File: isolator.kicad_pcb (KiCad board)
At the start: 4 copper layers, 120 x 50 mm, 54 parts, among them J1 HOST, J2 ISO_PORT, Q1 2N7002, T1 750313638, U1 ADuM4165, U2 USBLC6-2SC6, U3 USBLC6-2SC6, U4 SN6505BDBV, U5 TLV76750DGNR, U6 TPS2553DBV, Y1 24M 8pF

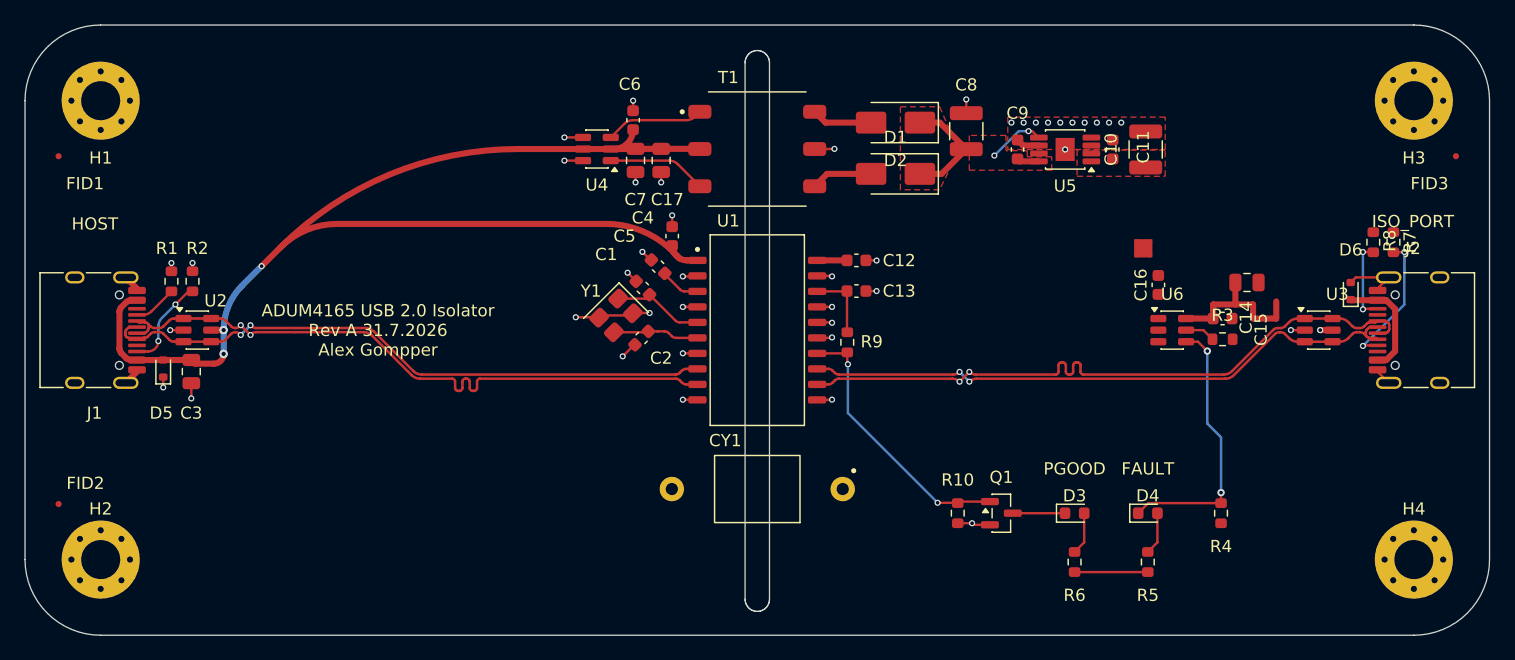
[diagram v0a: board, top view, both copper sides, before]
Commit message: wip: manual board re-import and placement pass
Hand work in the KiCad GUI after the C6 0805 change: schematic re-import,
board placement and routing. Committed as-is at Alex's request; not yet
re-verified against the gates.
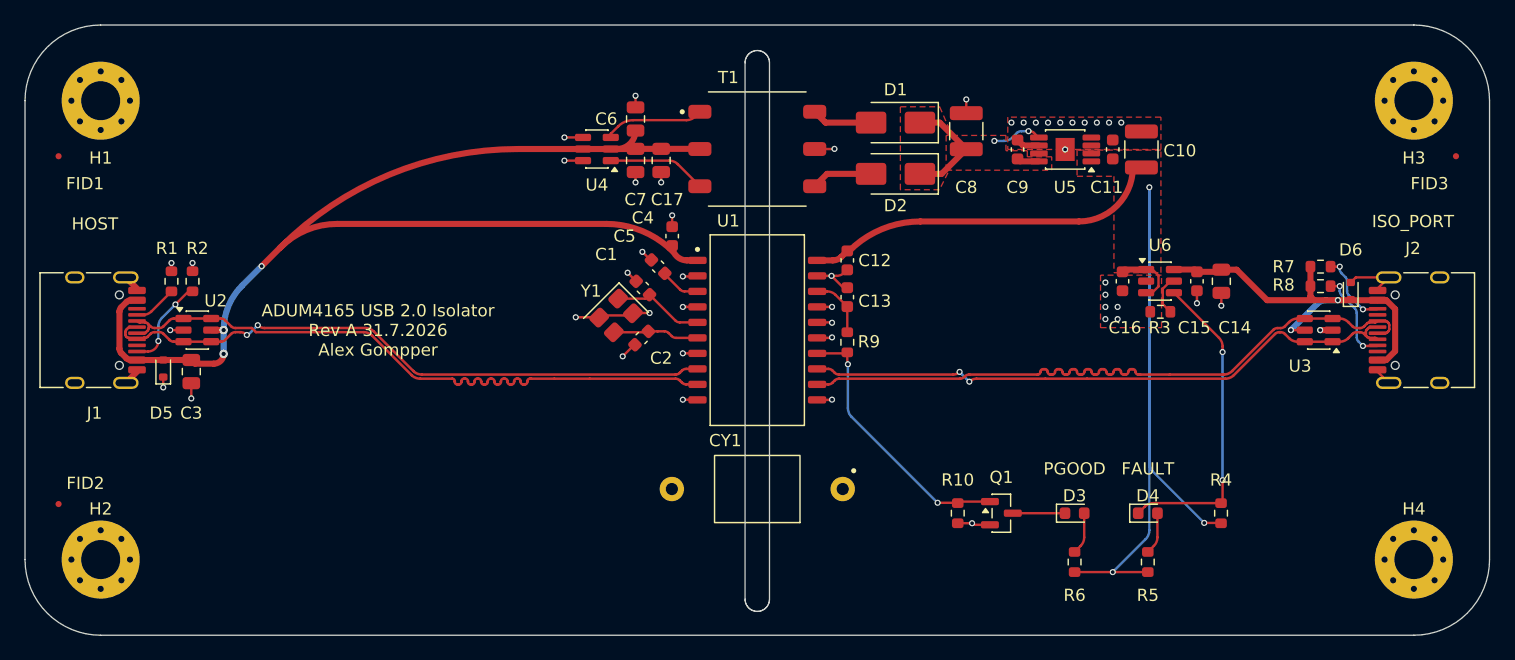
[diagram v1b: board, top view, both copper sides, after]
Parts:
- removed NT1: NetTie_4, NetTie:NetTie-4_SMD_Pad0.5mm
- removed NT3: NetTie_2, NetTie:NetTie-2_SMD_Pad0.5mm
- C6: footprint Capacitor_SMD:C_0603_1608Metric -> Capacitor_SMD:C_0805_2012Metric
- moved R7 6.30 mm to (193.0, 96.5), turned to 180 degrees
- moved R8 5.63 mm to (193.0, 98.1), turned to 0 degrees
- moved R3 5.57 mm to (179.9, 100.2)
- moved U6 4.14 mm to (179.9, 97.7)
- moved C15 3.71 mm to (182.9, 97.7), turned to -90 degrees
- moved C16 2.95 mm to (176.8, 97.7), turned to -90 degrees
- moved C14 2.10 mm to (184.9, 97.7), turned to -90 degrees
- moved C13 0.90 mm to (154.2, 99.0), turned to 90 degrees
- moved C12 0.75 mm to (154.2, 96.0), turned to -90 degrees
- moved C10 0.35 mm to (178.3, 86.9)
- moved C6 0.22 mm to (136.9, 84.4)
- turned R4 to -90 degrees
- turned U3 to 180 degrees
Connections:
- net /FAULT_LED_A renamed Net-(D4-A)
- C10 pad 1: /ISO_5V -> ISO_5V
- C11 pad 1: /ISO_5V -> ISO_5V
- C12 pad 1: /ISO_5V_VBUS2 -> ISO_5V
- C14 pad 1: /PORT_VBUS -> PORT_VBUS
- C15 pad 1: /PORT_VBUS -> PORT_VBUS
- C16 pad 1: /ISO_5V_SW -> ISO_5V
- D4 pad 1: /nFAULT -> Net-(D4-K)
- D6 pad 1: /PORT_VBUS_J2 -> PORT_VBUS
- J2 pad A4: /PORT_VBUS_J2 -> PORT_VBUS
- J2 pad A5: /PORT_CC1 -> Net-(J2-CC1)
- J2 pad A6: Net-(J2-D+-PadA6) -> /PORT_D+
- J2 pad A7: Net-(J2-D--PadA7) -> /PORT_D-
- J2 pad A9: /PORT_VBUS_J2 -> PORT_VBUS
- J2 pad B4: /PORT_VBUS_J2 -> PORT_VBUS
- J2 pad B5: /PORT_CC2 -> Net-(J2-CC2)
- J2 pad B6: Net-(J2-D+-PadA6) -> /PORT_D+
- J2 pad B7: Net-(J2-D--PadA7) -> /PORT_D-
- J2 pad B9: /PORT_VBUS_J2 -> PORT_VBUS
- R3 pad 1: /ILIM_SET -> GND2
- R3 pad 2: GND2 -> Net-(U6-ILIM)
- R4 pad 1: /ISO_5V_IND -> Net-(D4-K)
- R4 pad 2: /nFAULT -> ISO_5V
- R5 pad 1: /ISO_5V_IND -> ISO_5V
- R6 pad 1: /ISO_5V_IND -> ISO_5V
- R7 pad 1: /PORT_VBUS_J2 -> Net-(J2-CC2)
- R7 pad 2: /PORT_CC1 -> PORT_VBUS
- R8 pad 1: /PORT_VBUS_J2 -> PORT_VBUS
- R8 pad 2: /PORT_CC2 -> Net-(J2-CC1)
- U1 pad 20: /ISO_5V_VBUS2 -> ISO_5V
- U3 pad 1: Net-(J2-D--PadA7) -> /PORT_D-
- U3 pad 3: Net-(J2-D+-PadA6) -> /PORT_D+
- U3 pad 5: /PORT_VBUS_J2 -> PORT_VBUS
- U5 pad 1: /ISO_5V -> ISO_5V
- U5 pad 2: /ISO_5V -> ISO_5V
- U6 pad 1: /ISO_5V_SW -> ISO_5V
- U6 pad 3: /ISO_5V_SW -> ISO_5V
- U6 pad 4: /nFAULT -> Net-(D4-K)
- U6 pad 5: /ILIM_SET -> Net-(U6-ILIM)
- U6 pad 6: /PORT_VBUS -> PORT_VBUS
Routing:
- net ISO_5V: track 0.00 -> 102.4 mm, vias 0 -> 3
- net PORT_VBUS: track 0.00 -> 33.0 mm, vias 0 -> 2
- net Net-(D4-K): track 0.00 -> 25.8 mm, vias 0 -> 2
- net /nFAULT: track 22.1 -> 0.00 mm, vias 2 -> 0
- net /PORT_VBUS_J2: track 12.5 -> 0.00 mm, vias 1 -> 0
- net /PORT_CC1: track 11.2 -> 0.00 mm, vias 2 -> 0
- net /PORT_VBUS: track 9.59 -> 0.00 mm
- net Net-(J2-CC1): track 0.00 -> 7.52 mm, vias 0 -> 2
- net /PORT_CC2: track 6.78 -> 0.00 mm, vias 2 -> 0
- net Net-(J2-CC2): track 0.00 -> 6.12 mm, vias 0 -> 2
- net /ISO_5V_IND: track 6.00 -> 0.00 mm
- net Net-(U6-ILIM): track 0.00 -> 3.03 mm
- net GND2: track 22.3 -> 25.0 mm, vias 22 -> 28
- net /ILIM_SET: track 2.47 -> 0.00 mm
- net /ISO_5V_VBUS2: track 2.45 -> 0.00 mm
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- added copper zone on F.Cu, net ISO_5V
- removed copper zone on F.Cu, net /ISO_5V
